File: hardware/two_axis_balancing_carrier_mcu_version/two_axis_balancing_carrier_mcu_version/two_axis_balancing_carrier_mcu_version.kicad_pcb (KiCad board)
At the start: 4 copper layers, 101.6 x 92.9 mm, 31 parts, among them J1 Conn_01x03, J2 Conn_01x04, J5 Conn_02x05, U1 NUCLEO-G474RE, U2 MIC5219-3.3YM5, U3 ICM-42688-P, U4 SN65HVD230

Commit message: Started rev 2 of carrier board, mainly swapping the dev board for a bare mcu
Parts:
- removed 3.3V, 5V, CS, ENC_A, ENC_B, GND, INT1, INT2, RX, SCLK, SDI, SDO, TX: TestPoint, TestPoint:TestPoint_Pad_2.0x2.0mm
- removed REF** (x4): MountingHole_2.2mm_M2, MountingHole:MountingHole_2.2mm_M2
- added C10: 100nF, Capacitor_SMD:C_0603_1608Metric, F.Cu at (72.0, 29.0)
- added C11: 100nF, Capacitor_SMD:C_0603_1608Metric, F.Cu at (72.0, 24.9)
- added C12: 100nF, Capacitor_SMD:C_0603_1608Metric, F.Cu at (86.3, 21.6)
- added C13: 100nF, Capacitor_SMD:C_0603_1608Metric, F.Cu at (71.8, 21.8)
- added C14: 100nF, Capacitor_SMD:C_0603_1608Metric, F.Cu at (243.1, 22.3)
- added C15: 100nF, Capacitor_SMD:C_0603_1608Metric, F.Cu at (93.6, 25.3)
- added C16: 1uF, Capacitor_SMD:C_0805_2012Metric, F.Cu at (93.5, 29.5)
- added C17: 100nF, Capacitor_SMD:C_0603_1608Metric, F.Cu at (267.9, 20.0)
- added C18: 2.2uF, Capacitor_SMD:C_0805_2012Metric, F.Cu at (268.1, 22.4)
- added C19: 100pF, Capacitor_SMD:C_0603_1608Metric, F.Cu at (165.3, 25.9)
- added C20: 100pF, Capacitor_SMD:C_0603_1608Metric, F.Cu at (165.3, 27.6)
- added C21: 100nF, Capacitor_SMD:C_0603_1608Metric, F.Cu at (136.4, 31.2)
- added C7: 12pF, Capacitor_SMD:C_0603_1608Metric, F.Cu at (105.8, 30.9)
- added C8: 100nF, Capacitor_SMD:C_0603_1608Metric, F.Cu at (79.1, 28.6)
- added C9: 10nF, Capacitor_SMD:C_0603_1608Metric, F.Cu at (267.8, 16.7)
- added D1: LED, LED_SMD:LED_0603_1608Metric, F.Cu at (126.8, 20.2)
- added D2: LED, LED_SMD:LED_0603_1608Metric, F.Cu at (126.8, 22.8)
- added FB1: FerriteBead, Capacitor_SMD:C_0603_1608Metric, F.Cu at (79.1, 21.6)
- added FB2: FerriteBead, Capacitor_SMD:C_0603_1608Metric, F.Cu at (93.6, 21.4)
- added J3: Conn_01x04, Connector_JST:JST_GH_BM04B-GHS-TBT_1x04-1MP_P1.25mm_Vertical, F.Cu at (235.6, 27.9)
- added J4: Conn_01x04, Connector_JST:JST_XH_B4B-XH-A_1x04_P2.50mm_Vertical, F.Cu at (172.2, 27.2)
- added R2: 120R, Resistor_SMD:R_0603_1608Metric, F.Cu at (243.5, 18.3)
- added R3: 1kR, Resistor_SMD:R_0603_1608Metric, F.Cu at (117.4, 20.1)
- added R4: 1kR, Resistor_SMD:R_0603_1608Metric, F.Cu at (117.4, 22.6)
- added R5: 10kR, Resistor_SMD:R_0603_1608Metric, F.Cu at (117.4, 27.2)
- added R6: 10kR, Resistor_SMD:R_0603_1608Metric, F.Cu at (165.4, 20.0)
- added R7: 10kR, Resistor_SMD:R_0603_1608Metric, F.Cu at (165.4, 22.5)
- added TP1: TestPoint, TestPoint:TestPoint_Pad_2.0x2.0mm, F.Cu at (15.4, 15.3)
- added TP10: TestPoint, TestPoint:TestPoint_Pad_2.0x2.0mm, F.Cu at (19.5, 31.6)
- added TP11: TestPoint, TestPoint:TestPoint_Pad_2.0x2.0mm, F.Cu at (23.6, 15.3)
- added TP12: TestPoint, TestPoint:TestPoint_Pad_2.0x2.0mm, F.Cu at (23.6, 19.4)
- added TP13: TestPoint, TestPoint:TestPoint_Pad_2.0x2.0mm, F.Cu at (23.6, 23.4)
- added TP2: TestPoint, TestPoint:TestPoint_Pad_2.0x2.0mm, F.Cu at (15.4, 19.4)
- added TP3: TestPoint, TestPoint:TestPoint_Pad_2.0x2.0mm, F.Cu at (15.4, 23.4)
- added TP4: TestPoint, TestPoint:TestPoint_Pad_2.0x2.0mm, F.Cu at (15.4, 27.5)
- added TP5: TestPoint, TestPoint:TestPoint_Pad_2.0x2.0mm, F.Cu at (15.4, 31.6)
- added TP6: TestPoint, TestPoint:TestPoint_Pad_2.0x2.0mm, F.Cu at (19.5, 15.3)
- added TP7: TestPoint, TestPoint:TestPoint_Pad_2.0x2.0mm, F.Cu at (19.5, 19.4)
- added TP8: TestPoint, TestPoint:TestPoint_Pad_2.0x2.0mm, F.Cu at (19.5, 23.4)
- added TP9: TestPoint, TestPoint:TestPoint_Pad_2.0x2.0mm, F.Cu at (19.5, 27.5)
- added Y1: 8MHz, Crystal:Crystal_SMD_7050-4Pin_7.0x5.0mm, F.Cu at (104.8, 22.8)
- C3: value 100nF -> 4.7uF; footprint Capacitor_SMD:C_0603_1608Metric -> Capacitor_SMD:C_0805_2012Metric
- C4: value 10nF -> 1uF; footprint Capacitor_SMD:C_0603_1608Metric -> Capacitor_SMD:C_0805_2012Metric
- C6: value 2.2uF -> 12pF; footprint Capacitor_SMD:C_0805_2012Metric -> Capacitor_SMD:C_0603_1608Metric
- J1: value Conn_01x03 -> Conn_02x05; footprint Connector_JST:JST_GH_BM04B-GHS-TBT_1x04-1MP_P1.25mm_Vertical -> Connector_IDC:IDC-Header_2x05_P2.54mm_Vertical
- J2: value Conn_01x04 -> Conn_ST_STDC14; footprint Connector_JST:JST_XH_B4B-XH-A_1x04_P2.50mm_Vertical -> Connector_PinHeader_1.27mm:PinHeader_2x07_P1.27mm_Vertical
- J5: value Conn_02x05 -> Conn_02x08_Odd_Even; footprint Connector_IDC:IDC-Header_2x05_P2.54mm_Vertical -> Connector_PinHeader_2.54mm:PinHeader_2x08_P2.54mm_Vertical
- R1: value 120R -> 47R
- U1: value NUCLEO-G474RE -> MIC5219-3.3YM5; footprint NUCLEO-G474:MODULE_NUCLEO-G474RE -> Package_TO_SOT_SMD:SOT-23-5
- U2: value MIC5219-3.3YM5 -> ICM-42688-P; footprint Package_TO_SOT_SMD:SOT-23-5 -> ICM:LGA14_2P5X3X0P91_TDK
- U3: value ICM-42688-P -> SN65HVD230; footprint ICM:LGA14_2P5X3X0P91_TDK -> Package_SO:SOIC-8_3.9x4.9mm_P1.27mm
- U4: value SN65HVD230 -> STM32G474RETx; footprint Package_SO:SOIC-8_3.9x4.9mm_P1.27mm -> Package_QFP:LQFP-64_10x10mm_P0.5mm
- moved U2 144.2 mm to (262.6, 18.8)
- moved C4 124.9 mm to (79.0, 25.4), turned to 0 degrees
- moved J2 124.0 mm to (135.2, 19.5), turned to 0 degrees
- moved C5 123.9 mm to (72.3, 32.4), turned to 0 degrees
- moved C1 118.4 mm to (209.4, 21.8)
- moved C2 116.9 mm to (209.4, 19.2)
- moved C3 114.4 mm to (72.2, 36.9)
- moved U3 108.0 mm to (235.6, 20.3), turned to 0 degrees
- moved U1 104.3 mm to (203.5, 19.9)
- moved C6 103.2 mm to (105.8, 29.2), turned to 0 degrees
- moved J5 94.8 mm to (47.4, 18.4), turned to 0 degrees
- moved J1 84.8 mm to (103.0, 105.0)
- moved R1 79.3 mm to (106.1, 34.9)
- moved U4 53.9 mm to (130.0, 100.0), turned to 0 degrees
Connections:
- C1 pad 1: Net-(U2-BP) -> Net-(U1-BP)
- C4 pad 1: GND -> Net-(U4-VREF+)
- C4 pad 2: +3.3V -> GND
- C6 pad 1: +3.3V -> GND
- C6 pad 2: GND -> Net-(U4-PF0)
- J1 pad 1: GND -> +5V
- J1 pad 2: /CANL -> GND
- J1 pad 3: /CANH -> /BAT_LEV
- J1 pad 4: (no net) -> /BAT_LOW
- J2 pad 1: +5V -> unconnected-(J2-NC-Pad1)
- J2 pad 2: GND -> unconnected-(J2-NC-Pad2)
- J2 pad 3: /ENC_A -> +3.3V
- J2 pad 4: /ENC_B -> /DB_SWDIO
- J5 pad 1: +5V -> +3.3V
- J5 pad 10: GND -> /PC11
- J5 pad 2: GND -> +5V
- J5 pad 3: /BAT_LEV -> GND
- J5 pad 4: /BAT_LOW -> GND
- J5 pad 5: /STBY -> /PC8
- J5 pad 6: GND -> /PC9
- J5 pad 7: /AIN2 -> /PA9
- J5 pad 8: /AIN1 -> /PA10
- J5 pad 9: /PWMA -> /PC10
- R1 pad 1: /CANH -> Net-(C7-Pad2)
- R1 pad 2: /CANL -> Net-(U4-PF1)
- U2 pad 1: +5V -> /SDO
- U2 pad 3: +5V -> GND
- U2 pad 4: Net-(U2-BP) -> /INT1
- U3 pad 1: /SDO -> /CAN_TX
- U3 pad 3: GND -> +3.3V
- U3 pad 4: /INT1 -> /CAN_RX
- U3 pad 5: +3.3V -> unconnected-(U3-Vref-Pad5)
- U3 pad 6: GND -> /CANL
- U3 pad 7: GND -> /CANH
- U3 pad 8: +3.3V -> GND
- U4 pad 1: /TX -> +3.3V
- U4 pad 2: GND -> unconnected-(U4-PC13-Pad2)
- U4 pad 3: +3.3V -> unconnected-(U4-PC14-Pad3)
- U4 pad 4: /RX -> unconnected-(U4-PC15-Pad4)
- U4 pad 5: unconnected-(U4-Vref-Pad5) -> Net-(U4-PF0)
- U4 pad 6: /CANL -> Net-(U4-PF1)
- U4 pad 7: /CANH -> /DB_RESET
- U4 pad 8: GND -> /PWMA
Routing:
- net +5V: track 157.3 -> 0.00 mm
- net /ENC_A: track 98.0 -> 0.00 mm, vias 1 -> 0
- net /INT2: track 93.4 -> 0.00 mm, vias 2 -> 0
- net /INT1: track 87.6 -> 0.00 mm, vias 2 -> 0
- net +3.3V: track 69.8 -> 0.00 mm, vias 5 -> 0
- net /PWMA: track 61.7 -> 0.00 mm
- net /ENC_B: track 58.5 -> 0.00 mm, vias 1 -> 0
- net /BAT_LOW: track 40.4 -> 0.00 mm
- net /RX: track 39.4 -> 0.00 mm, vias 2 -> 0
- net /SDO: track 38.3 -> 0.00 mm, vias 2 -> 0
- net /AIN1: track 32.8 -> 0.00 mm
- net /TX: track 31.6 -> 0.00 mm, vias 2 -> 0
- net /BAT_LEV: track 31.6 -> 0.00 mm
- net /AIN2: track 30.1 -> 0.00 mm
- net /STBY: track 29.5 -> 0.00 mm
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- removed copper zone on B.Cu, net GND
- removed copper zone on F.Cu, net GND
- removed copper zone on In1.Cu, net GND
- removed copper zone on In2.Cu, net GND
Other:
- board size 101.6 x 92.9 mm -> 70 x 70 mm

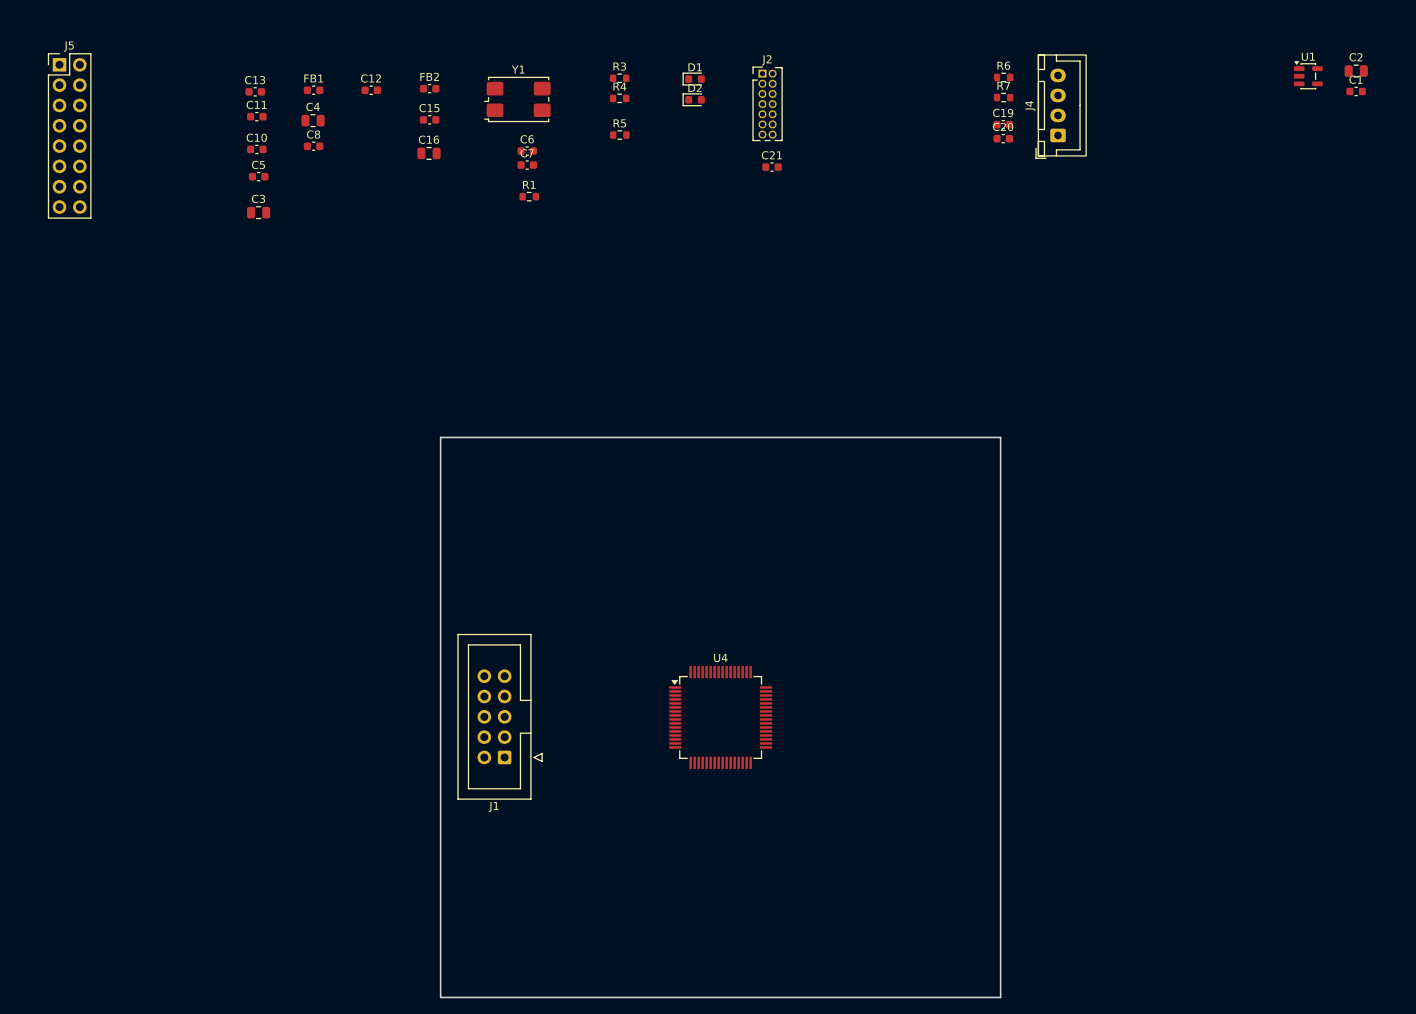
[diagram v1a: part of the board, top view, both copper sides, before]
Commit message: Changed crystal and progressed layout
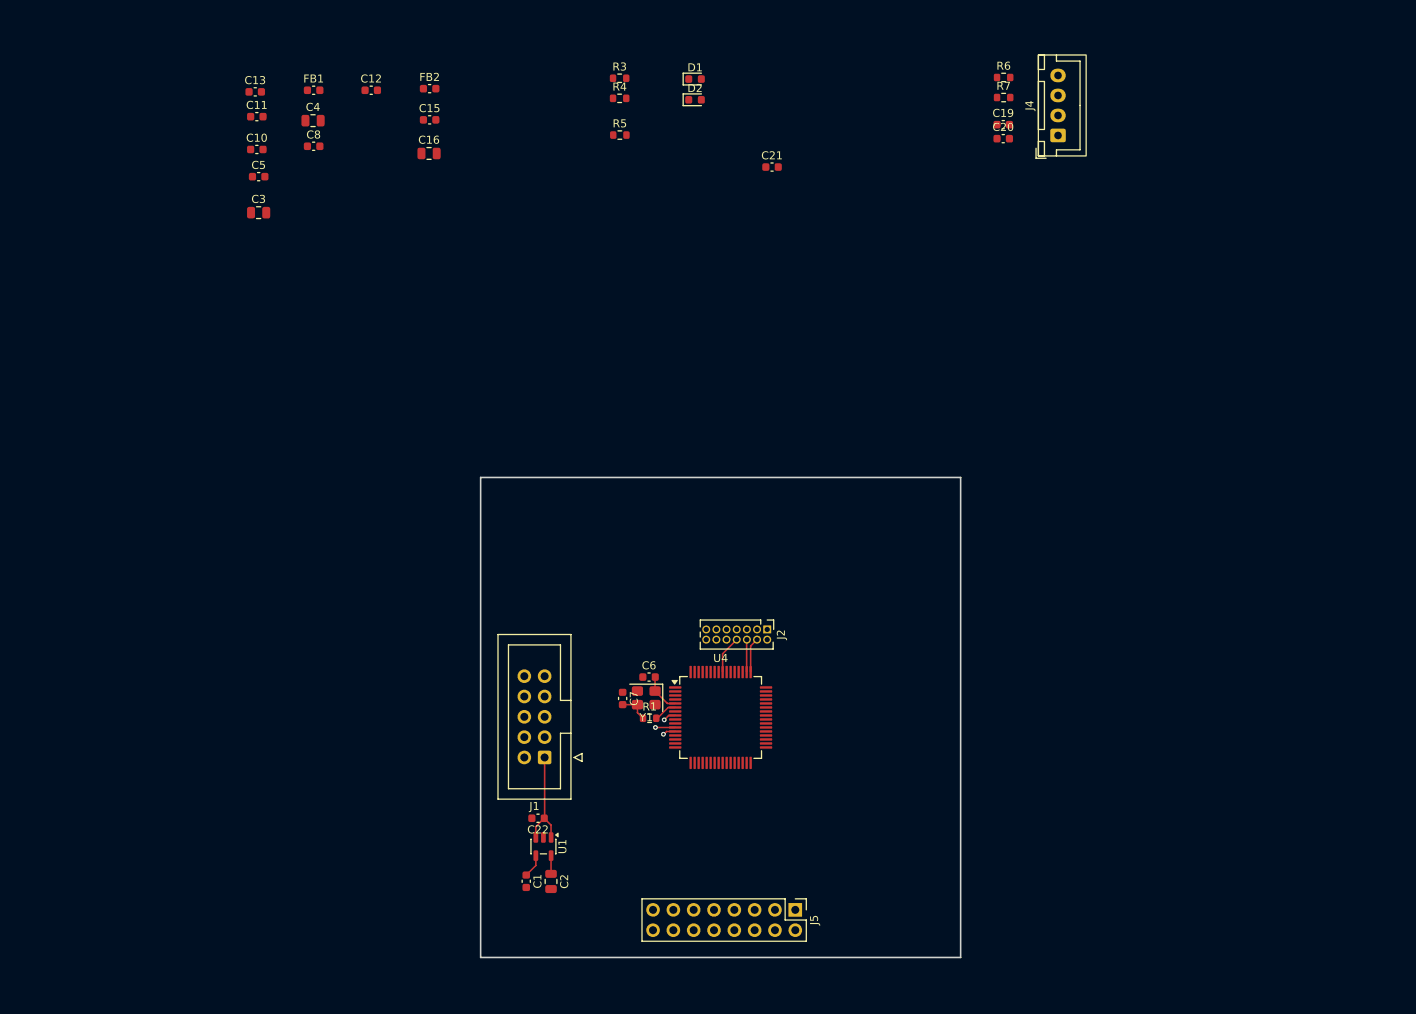
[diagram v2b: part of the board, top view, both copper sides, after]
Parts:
- added C22: 1uF, Capacitor_SMD:C_0603_1608Metric, F.Cu at (107.2, 112.6)
- Y1: footprint Crystal:Crystal_SMD_7050-4Pin_7.0x5.0mm -> Crystal:Crystal_SMD_3225-4Pin_3.2x2.5mm
- moved C1 143.2 mm to (105.7, 120.5), turned to -90 degrees
- moved C2 142.8 mm to (108.8, 120.5), turned to -90 degrees
- moved J5 140.1 mm to (139.3, 124.0), turned to -90 degrees
- moved U1 135.7 mm to (107.8, 116.1), turned to -90 degrees
- moved Y1 76.5 mm to (120.7, 97.5), turned to 180 degrees
- moved J2 69.5 mm to (135.8, 89.0), turned to -90 degrees
- moved C7 67.7 mm to (117.8, 97.6), turned to -90 degrees
- moved C6 67.5 mm to (121.0, 95.0)
- moved R1 66.9 mm to (121.1, 100.1)
- moved J1 5.00 mm to (108.0, 105.0)
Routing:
- net +5V: track 0.00 -> 13.2 mm
- net Net-(U4-PF0): track 0.00 -> 4.93 mm
- net /DB_SWO: track 0.00 -> 4.78 mm
- net /DB_SWDIO: track 0.00 -> 4.39 mm
- net /DB_SWCLK: track 0.00 -> 4.07 mm
- net Net-(C7-Pad2): track 0.00 -> 3.84 mm
- net Net-(U4-PF1): track 0.00 -> 2.93 mm
- net Net-(U1-BP): track 0.00 -> 2.92 mm
- net /BAT_LOW: track 0.00 -> 2.48 mm, vias 0 -> 1
- net +3.3V: track 0.00 -> 2.27 mm
- net /BAT_LEV: track 0.00 -> 1.62 mm, vias 0 -> 1
- net /PWMA: track 0.00 -> 1.60 mm, vias 0 -> 1
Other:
- board size 70 x 70 mm -> 60 x 60 mm

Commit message: Nearly finished layout and routing
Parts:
- moved C2 165.8 mm to (131.8, 111.5)
- moved C4 161.7 mm to (134.6, 113.7), turned to 180 degrees
- moved C3 161.5 mm to (134.8, 111.5), turned to 180 degrees
- moved U2 157.2 mm to (133.9, 109.1)
- moved C1 120.4 mm to (147.3, 95.2), turned to 180 degrees
- moved R1 117.0 mm to (147.5, 85.1)
- moved U1 112.8 mm to (147.5, 90.7), turned to 90 degrees
- moved FB2 109.0 mm to (138.3, 113.2)
- moved C11 106.7 mm to (141.1, 106.3)
- moved C16 104.4 mm to (138.6, 111.2)
- moved J1 101.3 mm to (148.7, 80.0)
- moved FB1 100.6 mm to (143.7, 108.7), turned to -90 degrees
- moved C12 100.5 mm to (128.1, 105.0), turned to 180 degrees
- moved C17 98.4 mm to (136.8, 108.4), turned to -90 degrees
- moved C8 94.9 mm to (117.2, 120.5), turned to -90 degrees
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- renumbered C14 to C1, C13 to C12, C12 to C13, C15 to C14, C16 to C15, C4 to C16, C8 to C17, C6 to C18, C7 to C19, C9 to C2, C21 to C20, C19 to C21, C20 to C22, C17 to C3, C18 to C4, C22 to C5, C2 to C6, C1 to C7, C3 to C8, C5 to C9, FB2 to FB1, FB1 to FB2, J3 to J1, J1 to J2, J4 to J3, J2 to J4, R2 to R1, R1 to R2, TP12 to TP10, TP6 to TP11, TP13 to TP12, TP7 to TP13, TP8 to TP2, TP2 to TP3, TP9 to TP4, TP3 to TP5, TP10 to TP6, TP4 to TP7, TP11 to TP8, TP5 to TP9, U3 to U1, U1 to U3
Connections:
- J5 pad 12: /PA8 -> /PB5
- R3 pad 1: Net-(U4-PB4) -> /LED_HB
- R4 pad 1: Net-(U4-PB5) -> /LED_FAULT
- U4 pad 38: unconnected-(U4-PC6-Pad38) -> /LED_HB
- U4 pad 42: /PA8 -> /LED_FAULT
- U4 pad 57: Net-(U4-PB4) -> unconnected-(U4-PB4-Pad57)
- U4 pad 58: Net-(U4-PB5) -> /PB5
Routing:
- net +3.3V: track 2.27 -> 30.9 mm, vias 0 -> 7
- net /DB_RESET: track 0.00 -> 18.3 mm, vias 0 -> 1
- net /ENC_B_PR: track 0.00 -> 12.7 mm
- net /INT2: track 0.00 -> 12.7 mm, vias 0 -> 2
- net /CAN_RX: track 0.00 -> 12.4 mm
- net /ENC_A_PR: track 0.00 -> 11.8 mm
- net /INT1: track 0.00 -> 10.2 mm, vias 0 -> 2
- net Net-(U4-PB8): track 0.00 -> 9.58 mm, vias 0 -> 2
- net /CS: track 0.00 -> 8.49 mm, vias 0 -> 2
- net Net-(U4-VREF+): track 0.00 -> 7.84 mm
- net /DB_RX: track 0.00 -> 7.62 mm
- net /CAN_TX: track 0.00 -> 7.15 mm
- net /CANL: track 0.00 -> 6.44 mm
- net /CANH: track 0.00 -> 6.39 mm
- net /SCLK: track 0.00 -> 4.30 mm, vias 0 -> 2
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- added copper zone on In2.Cu, net +3.3V
- added copper zone on B.Cu, net GND
- added copper zone on F.Cu, net GND
- added copper zone on In1.Cu, net GND
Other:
- board size 60 x 60 mm -> 50 x 50 mm

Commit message: nearly finished layout and routing
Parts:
- added C23: 100nF, Capacitor_SMD:C_0603_1608Metric, F.Cu at (126.8, 104.0)
- added TP14: TestPoint, TestPoint:TestPoint_Keystone_5015_Micro_Mini, F.Cu at (30.1, 16.1)
- TP1, TP10, TP11, TP12, TP13, TP2, TP3, TP4, TP6, TP7, TP8, TP9: footprint TestPoint:TestPoint_Pad_2.0x2.0mm -> TestPoint:TestPoint_Pad_D1.0mm
- TP5: footprint TestPoint:TestPoint_Pad_2.0x2.0mm -> TestPoint:TestPoint_Keystone_5015_Micro_Mini
- moved J5 21.7 mm to (124.4, 121.9), turned to 90 degrees
- moved C12 1.08 mm to (128.8, 105.8), turned to -90 degrees
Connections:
- J5 pad 10: /PC11 -> /PC9
- J5 pad 11: /PC12 -> /PA9
- J5 pad 12: /PB5 -> /PA10
- J5 pad 13: /PB10 -> /PC10
- J5 pad 14: /PB11 -> /PC11
- J5 pad 15: /PC4 -> /PC12
- J5 pad 16: /PC5 -> /PB5
- J5 pad 5: /PC8 -> /PC4
- J5 pad 6: /PC9 -> /PC5
- J5 pad 7: /PA9 -> /PB10
- J5 pad 8: /PA10 -> /PB11
- J5 pad 9: /PC10 -> /PC8
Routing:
- net +5V: track 13.2 -> 79.2 mm
- net /AIN1: track 0.00 -> 40.6 mm, vias 0 -> 1
- net /AIN2: track 0.00 -> 36.4 mm, vias 0 -> 1
- net /STBY: track 0.00 -> 32.3 mm, vias 0 -> 1
- net /PC4: track 0.00 -> 23.5 mm, vias 0 -> 1
- net /PC5: track 0.00 -> 21.5 mm, vias 0 -> 1
- net /PWMA: track 1.28 -> 21.9 mm, vias 1 -> 2
- net /BAT_LOW: track 2.54 -> 19.9 mm, vias 1 -> 2
- net /DB_TX: track 0.00 -> 17.0 mm, vias 0 -> 2
- net /BAT_LEV: track 1.62 -> 17.3 mm, vias 1 -> 2
- net /DB_RX: track 7.62 -> 17.7 mm, vias 0 -> 2
- net /INT2: track 12.7 -> 13.2 mm

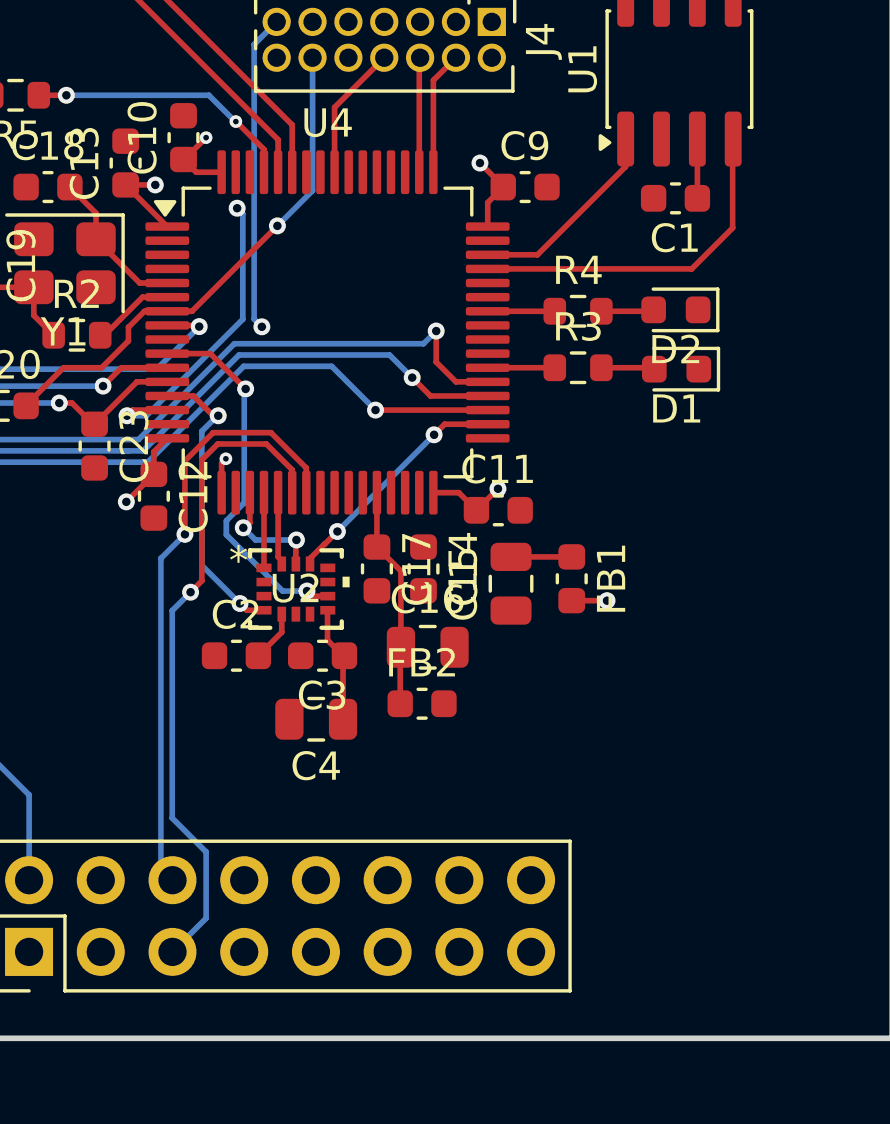
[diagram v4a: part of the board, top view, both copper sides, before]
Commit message: breakout header routing reworked
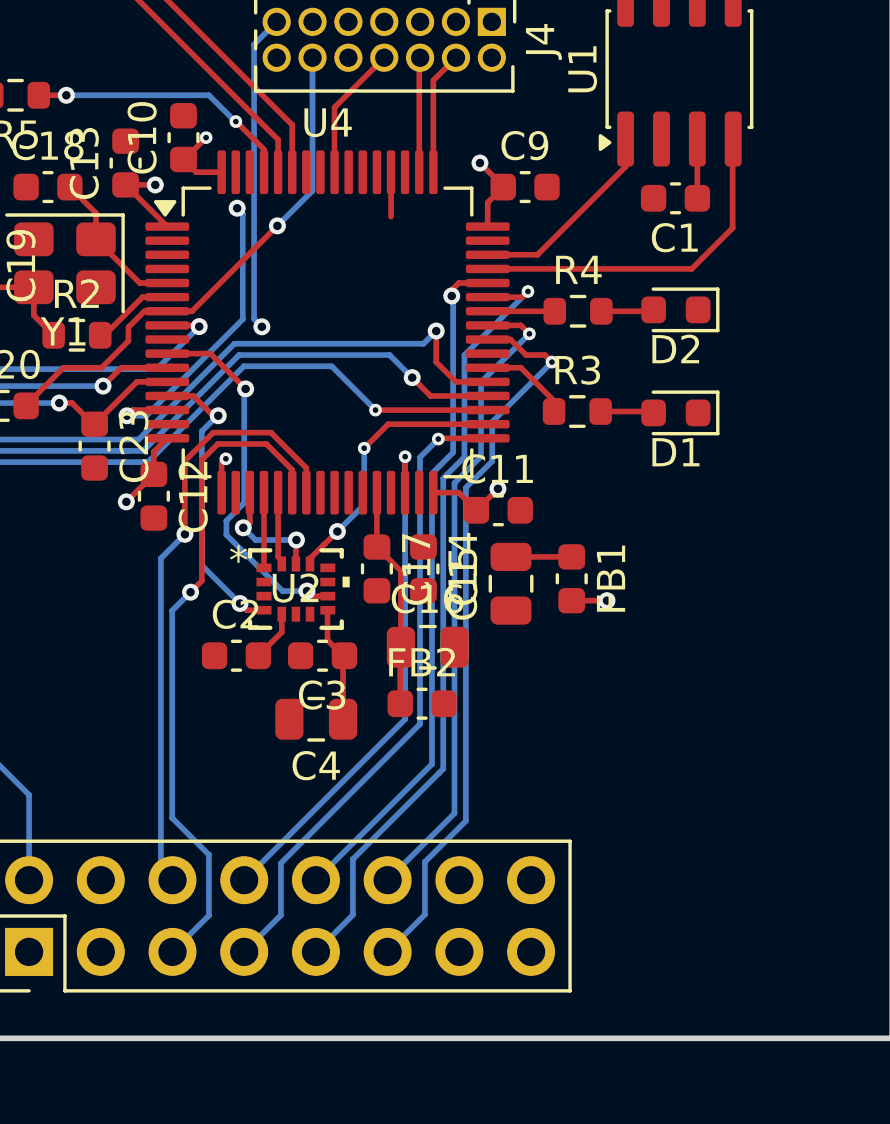
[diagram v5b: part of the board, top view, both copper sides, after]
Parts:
- moved D1 1.55 mm to (147.3, 102.8)
- moved R3 1.55 mm to (143.8, 102.8)
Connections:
- J5 pad 10: /PC9 -> /PA10
- J5 pad 11: /PA9 -> /PC8
- J5 pad 12: /PA10 -> /PC9
- J5 pad 7: /PB10 -> /PB11
- J5 pad 8: /PB11 -> /PB10
- J5 pad 9: /PC8 -> /PA9
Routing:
- net /PA9: track 0.00 -> 28.0 mm, vias 0 -> 1
- net /PC8: track 0.00 -> 25.9 mm, vias 0 -> 1
- net /PA10: track 0.00 -> 24.3 mm, vias 0 -> 1
- net /PC9: track 0.00 -> 23.8 mm, vias 0 -> 1
- net /PB11: track 0.00 -> 22.8 mm, vias 0 -> 1
- net /PB10: track 0.00 -> 18.6 mm, vias 0 -> 1
- net /PC10: track 0.00 -> 1.58 mm
- net /CS: track 8.46 -> 9.63 mm
- net /LED_HB: track 2.38 -> 3.21 mm
